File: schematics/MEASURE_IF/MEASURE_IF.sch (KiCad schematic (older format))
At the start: 0 parts

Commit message: Implement Depscan Interface Board
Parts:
- added A?: DRV8825_MOT1, Module:Pololu_Breakout-16_15.2x20.3mm, symbol Driver_Motor:Pololu_Breakout_DRV8825
- added A?: DRV8825_MOT2, Module:Pololu_Breakout-16_15.2x20.3mm, symbol Driver_Motor:Pololu_Breakout_DRV8825
- added C?: 1uF/25V/X5R, symbol Device:CP1_Small
- added C?: 10nF/X7R, symbol Device:CP1_Small
- added C? (x6): 100nF, symbol Device:C_Small
- added C?: 2.2uF, symbol Device:CP1_Small
- added C? (x2): 2.2uF/15V, symbol Device:CP1_Small
- added C? (x2): 22pF, symbol Device:C_Small
- added C?: 100uF/25V, symbol Device:CP1_Small
- added D? (x2): BAT60JFILM, symbol Device:D_Schottky_Small
- added FB? (x2): Ferrite_Bead_2012, symbol Device:Ferrite_Bead_Small
- added J?: USB_B_Micro, symbol Connector:USB_B_Micro
- added J?: ARGUS_SPI_LEGACY_CONN, Connector_PinHeader_1.27mm:CONN02x05CLOCKWISE, symbol Connector_Generic:Conn_02x05_Counter_Clockwise
- added J? (x4): MOT_TERM, symbol Connector:Screw_Terminal_01x02
- added J?: SWD_CONN, symbol Connector:Conn_01x06_Male
- added J?: ARGUS_SPI_FFC_CONN, symbol Connector:Conn_01x10_Male
- added J?: VMOT_IN_5mm, symbol Connector:Barrel_Jack
- added R?: 22k, symbol Device:R_US
- added SW?: SW_Push, symbol Switch:SW_Push
- added U?: USBLC6-2SC6, Package_TO_SOT_SMD:SOT-23-6, symbol Power_Protection:USBLC6-2SC6
- added U?: STM32G431KBTx, Package_QFP:LQFP-32_7x7mm_P0.8mm, symbol MCU_ST_STM32F3:STM32G431KBTx
- added U?: LD3985M33R_SOT23, Package_TO_SOT_SMD:SOT-23-5, symbol Regulator_Linear:LD3985M33R_SOT23
- added Y?: 24MHz, symbol Device:Crystal_Small
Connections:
- net labels added: +15V, ARGUS_CS, ARGUS_IRQ, BOOT0, GND, JTAG_SWO, MOT1_STEP, MOT2_STEP, MOT_DIR_1, MOT_DIR_2, MOTuCONF1, MOTuCONF2, NRST, OSC_IN, OSC_OUT, SPI_MISO, SPI_MOSI, SPI_SCK, STLINK_VIN, SWCLK, SWDIO, USB_DM, USB_DP, VBUS, VCC, VDD, VDDA, VSSA
- wire segments 3 -> 214
- no-connect marks 0 -> 13
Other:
- note added: "2.54mm Normal Pitch"
- note added: "MCU"
- note added: "MOTOR"
- note added: "MOTOR_PWR"
- note added: "PWR"
- note added: "SENSOR"
- note added: "SWD"
- note added: "USB"
- note added: "XTAL"

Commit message: Implement IF board artwork:
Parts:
- removed C?: 100uF/25V, symbol Device:CP1_Small
- removed J?: VMOT_IN_5mm, symbol Connector:Barrel_Jack
- removed SW?: SW_Push, symbol Switch:SW_Push
- added C14: 100uF/25V, Capacitor_SMD:CP_Elec_6.3x5.2, symbol Device:CP1_Small
- added D3: LED_G, LED_SMD:LED_0805_2012Metric, symbol Device:LED
- added D4: LED_Y, LED_SMD:LED_0805_2012Metric, symbol Device:LED
- added D5: LED_R, LED_SMD:LED_0805_2012Metric, symbol Device:LED
- added J4: VMOT_IN_5mm, Connector_BarrelJack:BarrelJack_Horizontal, symbol Connector:Barrel_Jack
- added JP1: BOOT0_JP, Connector_PinHeader_2.54mm:PinHeader_1x02_P2.54mm_Vertical, symbol Device:Jumper_NC_Small
- added JP2, JP3: CONF_FIX_JP, Jumper:SolderJumper-2_P1.3mm_Open_TrianglePad1.0x1.5mm, symbol Device:Jumper_NC_Small
- added R2: 22k, Resistor_SMD:R_0805_2012Metric_Pad1.15x1.40mm_HandSolder, symbol Device:R_US
- added R3, R4: 300, Resistor_SMD:R_0805_2012Metric_Pad1.15x1.40mm_HandSolder, symbol Device:R_Small_US
- added R5: 1k, Resistor_SMD:R_0805_2012Metric_Pad1.15x1.40mm_HandSolder, symbol Device:R_Small_US
- added R6: 22k, Resistor_SMD:R_0805_2012Metric_Pad1.15x1.40mm_HandSolder, symbol Device:R_Small_US
- added SW1: SW_RESET, Button_Switch_SMD:SW_SMD_TS1107, symbol Switch:SW_Push
- C1, C10, C11, C12, C13, C2, C3, C4, C5, C6, C7, C8, C9: renamed from C?; footprint (none) -> Capacitor_SMD:C_0805_2012Metric_Pad1.15x1.40mm_HandSolder
- D1, D2: renamed from D?; footprint (none) -> Diode_SMD:D_SOD-323
- FB1, FB2: renamed from FB?; footprint (none) -> Inductor_SMD:L_0805_2012Metric_Pad1.15x1.40mm_HandSolder
- J1: renamed from J?; footprint (none) -> Connector_PinHeader_2.54mm:PinHeader_2x03_P2.54mm_Vertical
- J3: renamed from J?; footprint (none) -> Connector_FFC-FPC:Hirose_FH12-10S-0.5SH_1x10-1MP_P0.50mm_Horizontal
- J5, J6, J8, J9: renamed from J?; footprint (none) -> TerminalBlock:TerminalBlock_bornier-2_P5.08mm
- J7: renamed from J?; footprint (none) -> Connector_USB:USB_Micro-B_Molex_47346-0001
- R1: renamed from R?; footprint (none) -> Resistor_SMD:R_0805_2012Metric_Pad1.15x1.40mm_HandSolder
- Y1: renamed from Y?; footprint (none) -> Crystal:Crystal_SMD_SeikoEpson_FA238V-4Pin_3.2x2.5mm_HandSoldering; symbol Device:Crystal_Small -> Device:Crystal_GND24_Small
- gave numbers to parts that had none: 6
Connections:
- net +15V: now also C14.1, J4.1, R5.1
- net BOOT0: now also JP1.1, R2.2
- net GND: now also Y1.2, Y1.4, D4.1 (K), R2.1, SW1.1; no longer A1.7 (GND), A2.7 (GND)
- net MOTuCONF1: now also JP2.1
- net MOTuCONF2: now also JP3.2
- net NRST: now also SW1.2
- net OSC_OUT: now also Y1.3; no longer Y1.2
- net SPI_MISO: now also J3.6 (Pin_6); no longer J3.5 (Pin_5)
- net SPI_MOSI: now also J3.5 (Pin_5); no longer J3.6 (Pin_6)
- net SWDIO: now also D3.1 (K)
- net VCC: now also R3.1, R4.1, R6.1
- net VDD: now also JP1.2
- new net: JP2.2, JP3.1, R6.2
- new net: D4.2 (A), R4.2
- new net: D5.2 (A), R5.2
- new net: D3.2 (A), R3.2
- new net GNDPWR: A1.7 (GND), A2.7 (GND), C14.2, D5.1 (K), J4.2
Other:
- note added: "All LEDs are 2012 metric"
- note added: "BOOT0"
- note added: "Default configuration\nis pull-down (from FLASH)"
- note added: "INDICATOR"
- moved on the sheet: A1, A2, C1, C10, C11, C12, C13, C2, C3, C4, C5, C6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

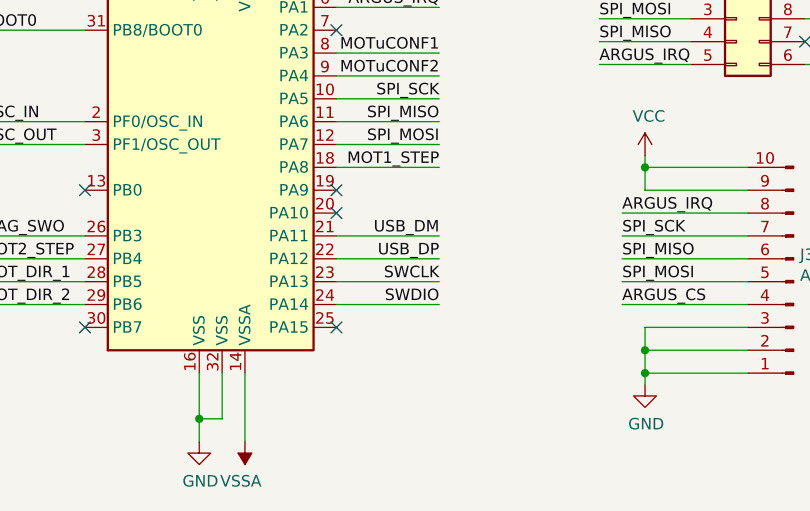
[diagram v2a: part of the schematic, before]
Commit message: Fix pin location error
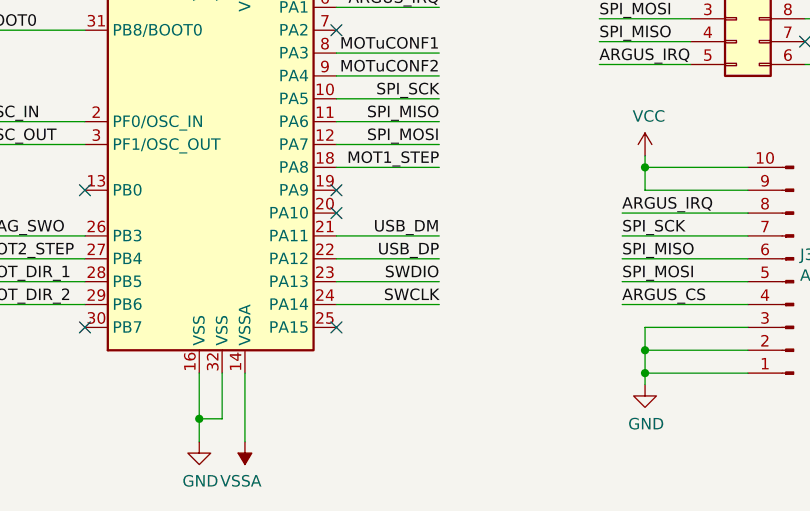
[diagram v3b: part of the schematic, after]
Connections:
- net SWCLK: now also U2.24 (PA14); no longer U2.23 (PA13)
- net SWDIO: now also U2.23 (PA13); no longer U2.24 (PA14)
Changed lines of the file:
@@
 $EndComp
 Text Label 4550 6300 2    50   ~ 0
+SWDIO
+Text Label 4550 6400 2    50   ~ 0
 SWCLK
-Text Label 4550 6400 2    50   ~ 0
-SWDIO
 Wire Wire Line
 	4100 6400 4550 6400

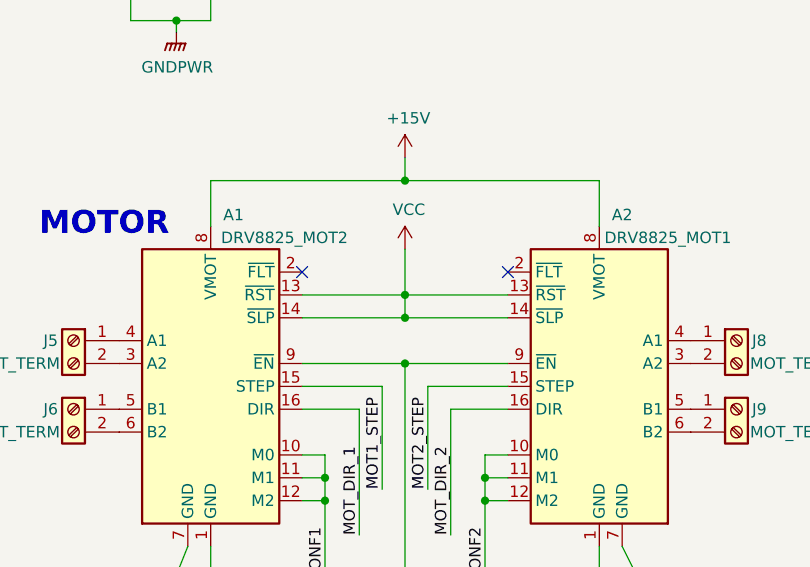
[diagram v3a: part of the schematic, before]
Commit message: Connect NRST signal to motor driver
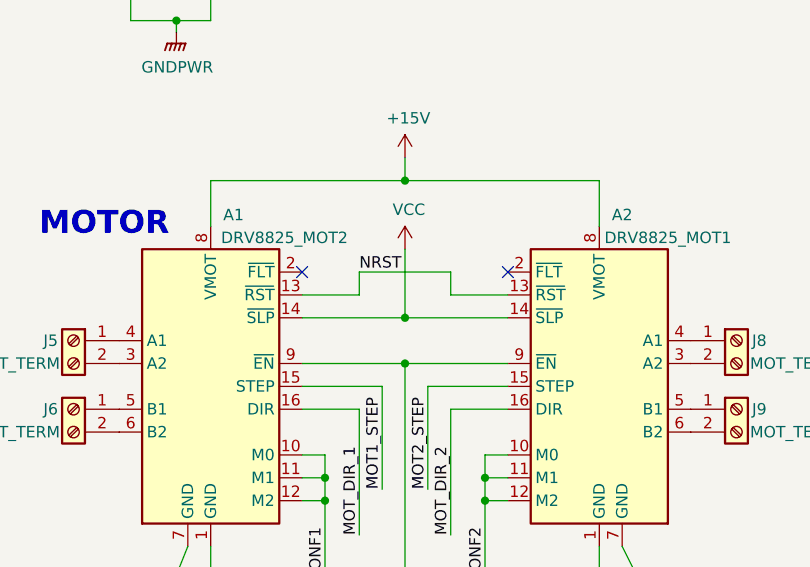
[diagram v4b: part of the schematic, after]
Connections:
- net NRST: now also A1.13 (~RST), A2.13 (~RST)
- net VCC: no longer A1.13 (~RST), A2.13 (~RST)
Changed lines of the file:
@@
 NoConn ~ 9400 4000
-Wire Wire Line
-	8500 4100 8950 4100
 Wire Wire Line
 	9400 4200 8950 4200
 NoConn ~ 8500 4000
-Wire Wire Line
-	8950 4200 8950 4100
 Connection ~ 8950 4200
 Wire Wire Line
 	8950 4200 8500 4200
-Connection ~ 8950 4100
-Wire Wire Line
-	8950 4100 9400 4100
 Wire Wire Line
 	9400 4400 8950 4400
@@
 	1    0    0    -1
 $EndComp
-Wire Wire Line
-	8950 3900 8950 4100
 $Comp
 L Device:Jumper_NC_Small JP2
@@
 Wire Wire Line
 	4450 3000 4450 3400
+Wire Wire Line
+	8950 3900 8950 4200
+Wire Wire Line
+	8750 4100 8750 4000
+Wire Wire Line
+	8750 4000 9150 4000
+Wire Wire Line
+	9150 4000 9150 4100
+Wire Wire Line
+	9150 4100 9400 4100
+Wire Wire Line
+	8500 4100 8750 4100
+Text Label 8750 4000 0    50   ~ 0
+NRST
 $EndSCHEMATC

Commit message: Change data communication method to ASCII
+ Originally data communication between the host and the device used
specialized data descriptor with 4 bytes of size.
However, this method prevents a user from using the device through a
primitive terminal program. Instead, it forces us to use a special
library that handles the protocol.
Since the data transmission rate of the USB-FS interface is outstanding
compared to other communication interfaces, I decided to represent
binary data as readable characters; '1-9', 'a-f'. Despite doubling its
data size.
Thus, for now, a user can access the device's commands without any
special library,  only with the method to access the virtual COM port
that is provided by ST.

--- PREVIOUS COMMIT MSG ---

Change module origin path

Apply

Revert "Apply"

This reverts commit bce002e20750f862fd87b41abe9ea4105aa8401c.

Apply library update

Implement firmware-side ASCII-only transfer

[wip] Unkown data corruption error

Fix data corruption erro

Implement ASCII based communication protocool
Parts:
- U2: symbol MCU_ST_STM32F3:STM32G431KBTx -> stm32custom:STM32G431KBTx
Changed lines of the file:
@@
 	2550 5200 3000 5200
 $Comp
-L MCU_ST_STM32F3:STM32G431KBTx U2
+L stm32custom:STM32G431KBTx U2
 U 1 1 5E3B8CB5
 P 3600 5700

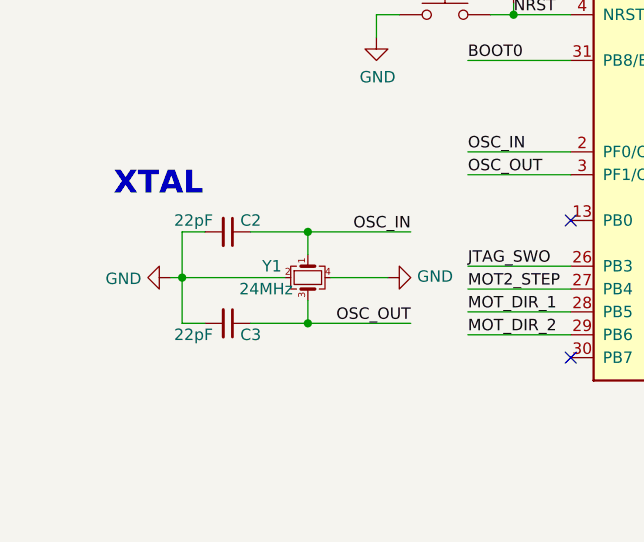
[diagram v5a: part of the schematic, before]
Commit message: Port overall system to G431KB based board
~ VID, PID is changed to 0x6080, 0xccd2 respectedly
- The build configuration for F401VC is now obsolete. Mamma mia!

---- PREVIOUS COMMITS ----

Remove unused project directory

- A separate project directory for G431KB is removed. From now on,
both F401VC and G431KB projects will be managed at the same time and
will have only minor differences in user code.

Configure build environment for G431KB

Configure build environment for G431KB

[WIP] Handling USB initialization error ...

[WIP]

Configure USB communication

Verify USB/Sensor operation

Update .gitignore

Verify USB/Sensor operation

Fix motor position error

Report different type of time for each status
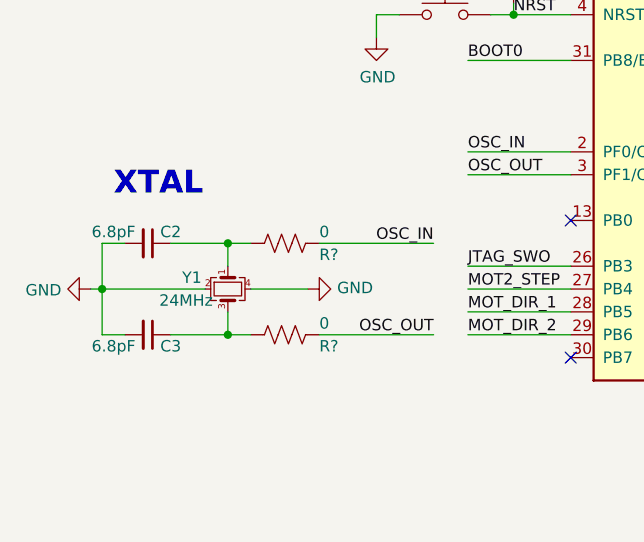
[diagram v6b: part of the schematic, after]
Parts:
- added R? (x2): 0, Resistor_SMD:R_0805_2012Metric_Pad1.15x1.40mm_HandSolder, symbol Device:R_US
- C2, C3: value 22pF -> 6.8pF
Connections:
- net OSC_IN: now also R?.1; no longer C2.1, Y1.1
- net OSC_OUT: now also R?.1; no longer C3.1, Y1.3
- new net: C2.1, R?.2, Y1.1
- new net: C3.1, R?.2, Y1.3
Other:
- moved on the sheet: C2, C3, Y1
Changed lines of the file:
@@
 Connection ~ 8950 3600
 Wire Wire Line
-	1300 6150 1300 6350
-Connection ~ 1300 6150
-Wire Wire Line
-	1250 6150 1300 6150
+	950  6200 950  6400
+Connection ~ 950  6200
+Wire Wire Line
+	900  6200 950  6200
 $Comp
 L power:GND #PWR02
 U 1 1 5E6D2E23
-P 1250 6150
-F 0 "#PWR02" H 1250 5900 50  0001 C CNN
-F 1 "GND" V 1255 6022 50  0000 R CNN
-F 2 "" H 1250 6150 50  0001 C CNN
-F 3 "" H 1250 6150 50  0001 C CNN
-	1    1250 6150
+P 900 6200
+F 0 "#PWR02" H 900 5950 50  0001 C CNN
+F 1 "GND" V 905 6072 50  0000 R CNN
+F 2 "" H 900 6200 50  0001 C CNN
+F 3 "" H 900 6200 50  0001 C CNN
+	1    900  6200
 	0    1    1    0
 $EndComp
 Wire Wire Line
-	1300 5950 1300 6150
-Wire Wire Line
-	1300 5950 1400 5950
-Wire Wire Line
-	1400 6350 1300 6350
-Wire Wire Line
-	1850 6350 1600 6350
+	950  6000 950  6200
+Wire Wire Line
+	950  6000 1050 6000
+Wire Wire Line
+	1050 6400 950  6400
+Wire Wire Line
+	1500 6400 1250 6400
 $Comp
 L Device:C_Small C3
 U 1 1 5E6B4D27
-P 1500 6350
-F 0 "C3" V 1550 6450 50  0000 C CNN
-F 1 "22pF" V 1550 6200 50  0000 C CNN
-F 2 "Capacitor_SMD:C_0805_2012Metric_Pad1.15x1.40mm_HandSolder" H 1500 6350 50  0001 C CNN
-F 3 "~" H 1500 6350 50  0001 C CNN
-	1    1500 6350
+P 1150 6400
+F 0 "C3" V 1200 6500 50  0000 C CNN
+F 1 "6.8pF" V 1200 6250 50  0000 C CNN
+F 2 "Capacitor_SMD:C_0805_2012Metric_Pad1.15x1.40mm_HandSolder" H 1150 6400 50  0001 C CNN
+F 3 "~" H 1150 6400 50  0001 C CNN
+	1    1150 6400
 	0    1    1    0
 $EndComp
 Wire Wire Line
-	1600 5950 1850 5950
-$Comp
-L Device:C_Small C2
-U 1 1 5E6AC17F
-P 1500 5950
-F 0 "C2" V 1450 6050 50  0000 C CNN
-F 1 "22pF" V 1450 5800 50  0000 C CNN
-F 2 "Capacitor_SMD:C_0805_2012Metric_Pad1.15x1.40mm_HandSolder" H 1500 5950 50  0001 C CNN
-F 3 "~" H 1500 5950 50  0001 C CNN
-	1    1500 5950
-	0    1    1    0
-$EndComp
-Wire Wire Line
-	1850 6050 1850 5950
+	1250 6000 1500 6000
+Wire Wire Line
+	1500 6100 1500 6000
 Wire Wire Line
 	2550 5700 3000 5700
 Wire Wire Line
 	2550 5600 3000 5600
-Text Label 2300 5950 2    50   ~ 0
+Text Label 2400 6000 2    50   ~ 0
 OSC_IN
-Wire Wire Line
-	2300 5950 1850 5950
-Connection ~ 1850 5950
-Wire Wire Line
-	1850 6350 1850 6250
-Wire Wire Line
-	2300 6350 1850 6350
-Text Label 2300 6350 2    50   ~ 0
+Connection ~ 1500 6000
+Wire Wire Line
+	1500 6400 1500 6300
+Text Label 2400 6400 2    50   ~ 0
 OSC_OUT
-Connection ~ 1850 6350
+Connection ~ 1500 6400
 $Comp
 L power:VCC #PWR033
@@
 L Device:Crystal_GND24_Small Y1
 U 1 1 5E6882FB
-P 1850 6150
-F 0 "Y1" V 1800 5950 50  0000 L CNN
-F 1 "24MHz" V 1900 5850 50  0000 L CNN
-F 2 "Crystal:Crystal_SMD_SeikoEpson_FA238V-4Pin_3.2x2.5mm_HandSoldering" H 1850 6150 50  0001 C CNN
-F 3 "~" H 1850 6150 50  0001 C CNN
-	1    1850 6150
+P 1500 6200
+F 0 "Y1" V 1450 6000 50  0000 L CNN
+F 1 "24MHz" V 1550 5900 50  0000 L CNN
+F 2 "Crystal:Crystal_SMD_SeikoEpson_FA238V-4Pin_3.2x2.5mm_HandSoldering" H 1500 6200 50  0001 C CNN
+F 3 "~" H 1500 6200 50  0001 C CNN
+	1    1500 6200
 	0    1    1    0
 $EndComp
 Wire Wire Line
-	1750 6150 1300 6150
+	1400 6200 950  6200
 $Comp
 L power:GND #PWR06
 U 1 1 5EB655F6
-P 2200 6150
-F 0 "#PWR06" H 2200 5900 50  0001 C CNN
-F 1 "GND" V 2205 6022 50  0000 R CNN
-F 2 "" H 2200 6150 50  0001 C CNN
-F 3 "" H 2200 6150 50  0001 C CNN
-	1    2200 6150
+P 1850 6200
+F 0 "#PWR06" H 1850 5950 50  0001 C CNN
+F 1 "GND" V 1855 6072 50  0000 R CNN
+F 2 "" H 1850 6200 50  0001 C CNN
+F 3 "" H 1850 6200 50  0001 C CNN
+	1    1850 6200
 	0    -1   -1   0
 $EndComp
 Wire Wire Line
-	2200 6150 1950 6150
+	1850 6200 1600 6200
 $Comp
 L power:GNDPWR #PWR024
@@
 Text Label 8750 4000 0    50   ~ 0
 NRST
+$Comp
+L Device:R_US R?
+U 1 1 5E4F7F7D
+P 1750 6000
+F 0 "R?" V 1800 6150 50  0000 L CNN
+F 1 "0" V 1700 6150 50  0000 L CNN
+F 2 "Resistor_SMD:R_0805_2012Metric_Pad1.15x1.40mm_HandSolder" V 1790 5990 50  0001 C CNN
+F 3 "~" H 1750 6000 50  0001 C CNN
+	1    1750 6000
+	0    1    1    0
+$EndComp
+$Comp
+L Device:R_US R?
+U 1 1 5E4F8A6C
+P 1750 6400
+F 0 "R?" V 1800 6550 50  0000 L CNN
+F 1 "0" V 1700 6550 50  0000 L CNN
+F 2 "Resistor_SMD:R_0805_2012Metric_Pad1.15x1.40mm_HandSolder" V 1790 6390 50  0001 C CNN
+F 3 "~" H 1750 6400 50  0001 C CNN
+	1    1750 6400
+	0    1    1    0
+$EndComp
+Wire Wire Line
+	1500 6400 1600 6400
+Wire Wire Line
+	1500 6000 1600 6000
+Wire Wire Line
+	2400 6000 1900 6000
+$Comp
+L Device:C_Small C2
+U 1 1 5E6AC17F
+P 1150 6000
+F 0 "C2" V 1100 6100 50  0000 C CNN
+F 1 "6.8pF" V 1100 5850 50  0000 C CNN
+F 2 "Capacitor_SMD:C_0805_2012Metric_Pad1.15x1.40mm_HandSolder" H 1150 6000 50  0001 C CNN
+F 3 "~" H 1150 6000 50  0001 C CNN
+	1    1150 6000
+	0    1    1    0
+$EndComp
+Wire Wire Line
+	1900 6400 2400 6400
 $EndSCHEMATC
